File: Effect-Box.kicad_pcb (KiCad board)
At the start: 6 copper layers, 178.6 x 140 mm, 161 parts, among them J1 Conn_02x07_Odd_Even, J10 Power pins, J2 26642801RP2, J3 FH12A-10S-0.5SH55, J5 Conn_ARM_JTAG_SWD_20, J6 26642801RP2, J7 AudioJack3, J8 AudioJack3, J9 PJ-006A-SMT, SW0 SW_Push, SW1 SW_Push, SW2 SW_Push, SW3 SW_Push, SW4 SW_Push, SW5 SW_Push, SW6 SW_Push, U1 TPS54325, U10 LM7805SX_NOPB, U2 TPS54294, U3 XC7A100T-FTG256, U4 S25FL1, U5 SiT2024B, U7 EFM32GG942F1024, U8 INA1651IPW, U9 PCM3003E

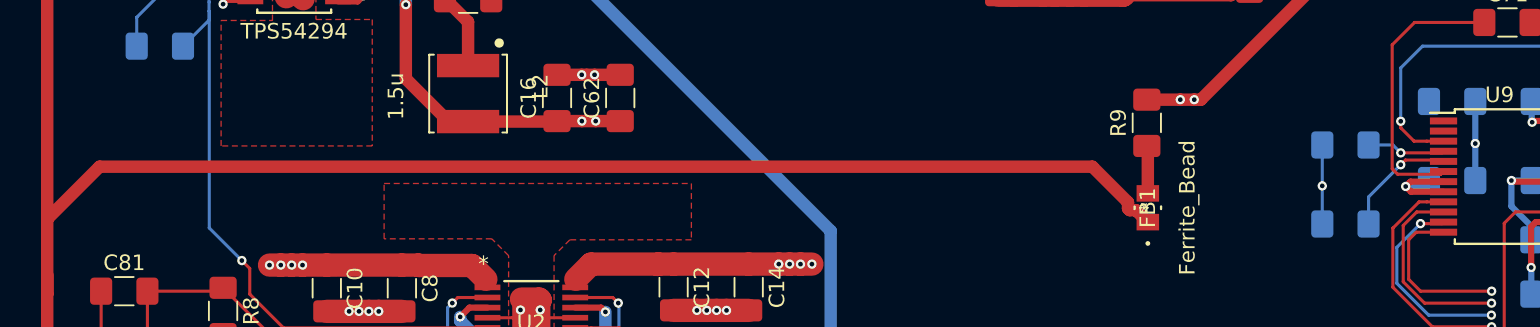
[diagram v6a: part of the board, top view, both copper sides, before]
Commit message: Fix audio part errors
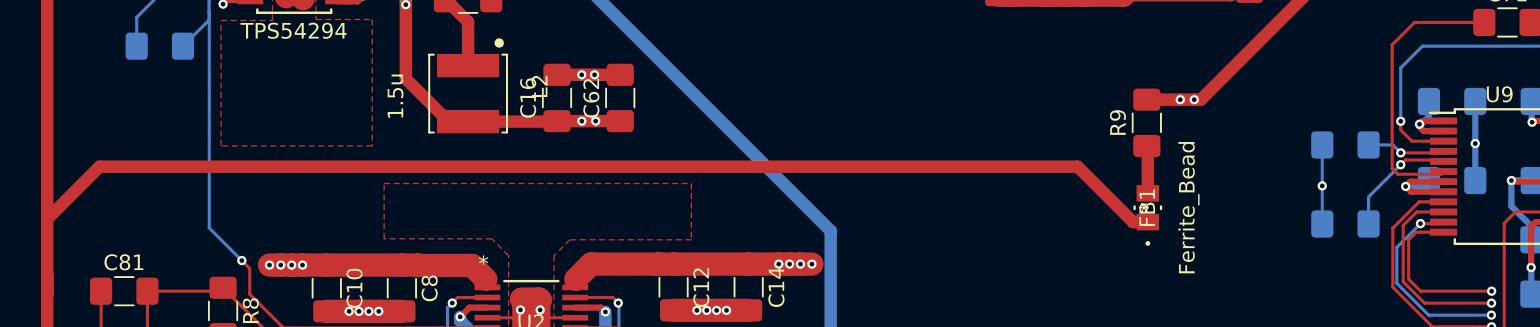
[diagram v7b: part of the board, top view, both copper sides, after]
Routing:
- net +3.3VA: track 121.0 -> 126.3 mm, vias 7 -> 8
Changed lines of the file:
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@@
     (thickness 1.6)
     (drawings 3522)
-    (tracks 2350)
+    (tracks 2356)
     (zones 0)
     (modules 161)
@@
   )
   (setup
-    (last_trace_width 0.2)
+    (last_trace_width 0.4)
     (user_trace_width 0.2)
     (user_trace_width 0.4)
@@
   (segment (start 147.247 69.7325) (end 148.5805 69.7325) (width 0.8) (layer F.Cu) (net 14))
   (segment (start 148.644 69.7325) (end 151.184 69.7325) (width 0.8) (layer F.Cu) (net 14))
-  (segment (start 144.4625 52.705) (end 141.097 56.0705) (width 0.8) (layer F.Cu) (net 14))
-  (segment (start 208.2729 52.705) (end 144.4625 52.705) (width 0.8) (layer F.Cu) (net 14))
-  (segment (start 211.068001 55.500101) (end 210.672099 55.500101) (width 0.8) (layer F.Cu) (net 14))
-  (segment (start 211.836 56.2681) (end 211.068001 55.500101) (width 0.8) (layer F.Cu) (net 14))
-  (segment (start 210.562099 55.390101) (end 210.562099 54.994199) (width 0.8) (layer F.Cu) (net 14))
-  (segment (start 210.672099 55.500101) (end 210.562099 55.390101) (width 0.8) (layer F.Cu) (net 14))
-  (segment (start 210.562099 54.994199) (end 208.2729 52.705) (width 0.8) (layer F.Cu) (net 14))
   (via (at 209.931 110.1725) (size 0.6) (drill 0.3) (layers F.Cu B.Cu) (net 14))
   (segment (start 211.2645 110.1725) (end 209.931 110.1725) (width 0.4) (layer F.Cu) (net 14))
@@
   (segment (start 148.5805 69.7325) (end 148.644 69.7325) (width 0.8) (layer F.Cu) (net 14))
   (via (at 148.5805 69.7325) (size 0.6) (drill 0.3) (layers F.Cu B.Cu) (net 14))
+  (segment (start 144.4625 52.705) (end 141.097 56.0705) (width 0.8) (layer F.Cu) (net 14))
+  (segment (start 207.3275 52.705) (end 144.4625 52.705) (width 0.8) (layer F.Cu) (net 14))
+  (segment (start 211.836 56.2681) (end 210.8906 56.2681) (width 0.8) (layer F.Cu) (net 14))
+  (segment (start 210.8906 56.2681) (end 207.3275 52.705) (width 0.8) (layer F.Cu) (net 14))
   (segment (start 146.8485 43.107) (end 149.8235 40.132) (width 0.2) (layer B.Cu) (net 15))
   (segment (start 146.8485 44.958) (end 146.8485 43.107) (width 0.2) (layer B.Cu) (net 15))
@@
   (segment (start 214.8205 48.3965) (end 215.244764 48.3965) (width 0.8) (layer F.Cu) (net 21))
   (segment (start 169.22751 22.28849) (end 226.207236 22.28849) (width 0.8) (layer B.Cu) (net 21))
+  (via (at 229.2985 49.974522) (size 0.6) (drill 0.3) (layers F.Cu B.Cu) (net 21))
+  (segment (start 229.508022 49.765) (end 229.2985 49.974522) (width 0.4) (layer F.Cu) (net 21))
+  (segment (start 229.567 50.415) (end 229.2985 50.1465) (width 0.4) (layer F.Cu) (net 21))
+  (segment (start 229.2985 50.1465) (end 229.2985 49.974522) (width 0.4) (layer F.Cu) (net 21))
+  (segment (start 230.842 50.415) (end 229.567 50.415) (width 0.4) (layer F.Cu) (net 21))
+  (segment (start 229.420978 49.974522) (end 229.2985 49.974522) (width 0.4) (layer B.Cu) (net 21))
+  (segment (start 229.9065 48.514) (end 229.9065 49.489) (width 0.4) (layer B.Cu) (net 21))
+  (segment (start 230.842 49.765) (end 229.508022 49.765) (width 0.4) (layer F.Cu) (net 21))
+  (segment (start 229.9065 49.489) (end 229.420978 49.974522) (width 0.4) (layer B.Cu) (net 21))
   (segment (start 236.4375 43.434) (end 241.046 38.8255) (width 0.2) (layer F.Cu) (net 22))
   (segment (start 241.046 38.8255) (end 241.046 32.512) (width 0.2) (layer F.Cu) (net 22))
@@
   (segment (start 242.57 50.292) (end 241.3 51.562) (width 0.2) (layer B.Cu) (net 26))
   (via (at 228.092 49.784) (size 0.6) (drill 0.3) (layers F.Cu B.Cu) (net 26))
-  (segment (start 229.767 51.065) (end 230.842 51.065) (width 0.2) (layer F.Cu) (net 26))
-  (segment (start 228.948736 51.065) (end 229.767 51.065) (width 0.2) (layer F.Cu) (net 26))
-  (segment (start 228.092 50.208264) (end 228.948736 51.065) (width 0.2) (layer F.Cu) (net 26))
-  (segment (start 228.092 49.784) (end 228.092 50.208264) (width 0.2) (layer F.Cu) (net 26))
   (segment (start 229.489 44.958) (end 228.092 46.355) (width 0.2) (layer B.Cu) (net 26))
   (segment (start 239.268 44.958) (end 229.489 44.958) (width 0.2) (layer B.Cu) (net 26))
@@
   (segment (start 241.000001 51.861999) (end 238.188999 51.861999) (width 0.2) (layer F.Cu) (net 26))
   (segment (start 241.3 51.562) (end 241.000001 51.861999) (width 0.2) (layer F.Cu) (net 26))
+  (segment (start 228.092 50.344002) (end 228.812998 51.065) (width 0.2) (layer F.Cu) (net 26))
+  (segment (start 228.092 49.784) (end 228.092 50.344002) (width 0.2) (layer F.Cu) (net 26))
+  (segment (start 228.812998 51.065) (end 229.767 51.065) (width 0.2) (layer F.Cu) (net 26))
+  (segment (start 229.767 51.065) (end 230.842 51.065) (width 0.2) (layer F.Cu) (net 26))
   (via (at 260.858 60.452) (size 0.6) (drill 0.3) (layers F.Cu B.Cu) (net 27))
   (segment (start 247.3595 60.452) (end 260.858 60.452) (width 0.2) (layer B.Cu) (net 27))

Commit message: Fix MCU
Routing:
- net GND: track 355.2 -> 340.3 mm, vias 217 -> 220
- net Net-(J5-Pad13): track 34.6 -> 36.2 mm
- net +3V3: track 288.8 -> 288.0 mm
